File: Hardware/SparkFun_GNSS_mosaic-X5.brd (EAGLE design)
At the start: 63.5 x 50.8 mm, 189 parts, among them J3 MICROSD, J5 USB Female Type C Connector, Q9 20V/0.2A/8MHz/1.2Ω/1Vth, T1 RFCMF1220100M4T, U1 MOSAIC-X5X5, U2 SN74AHC1G125DBVR, U5 3.3V

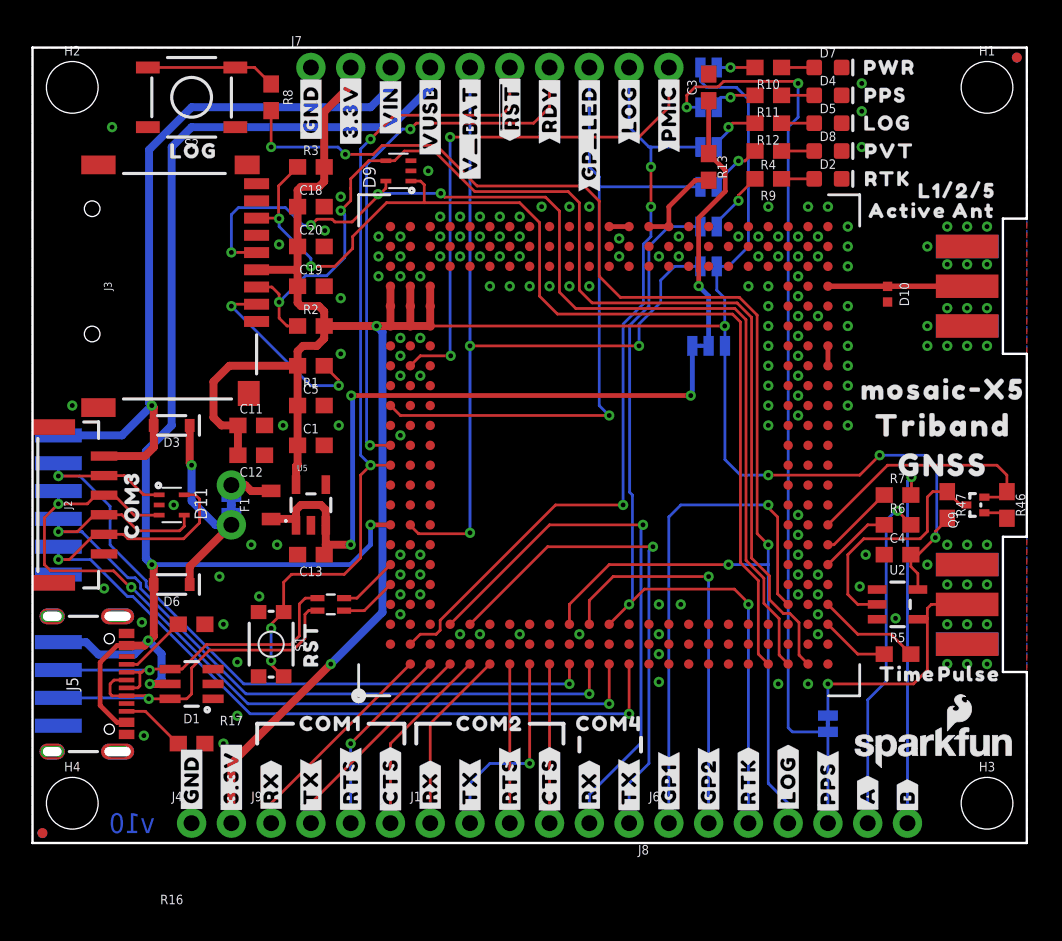
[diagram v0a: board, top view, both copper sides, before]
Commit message: Fix 1.8V net, fix silk, add more ESD protection, add LOG pullup.
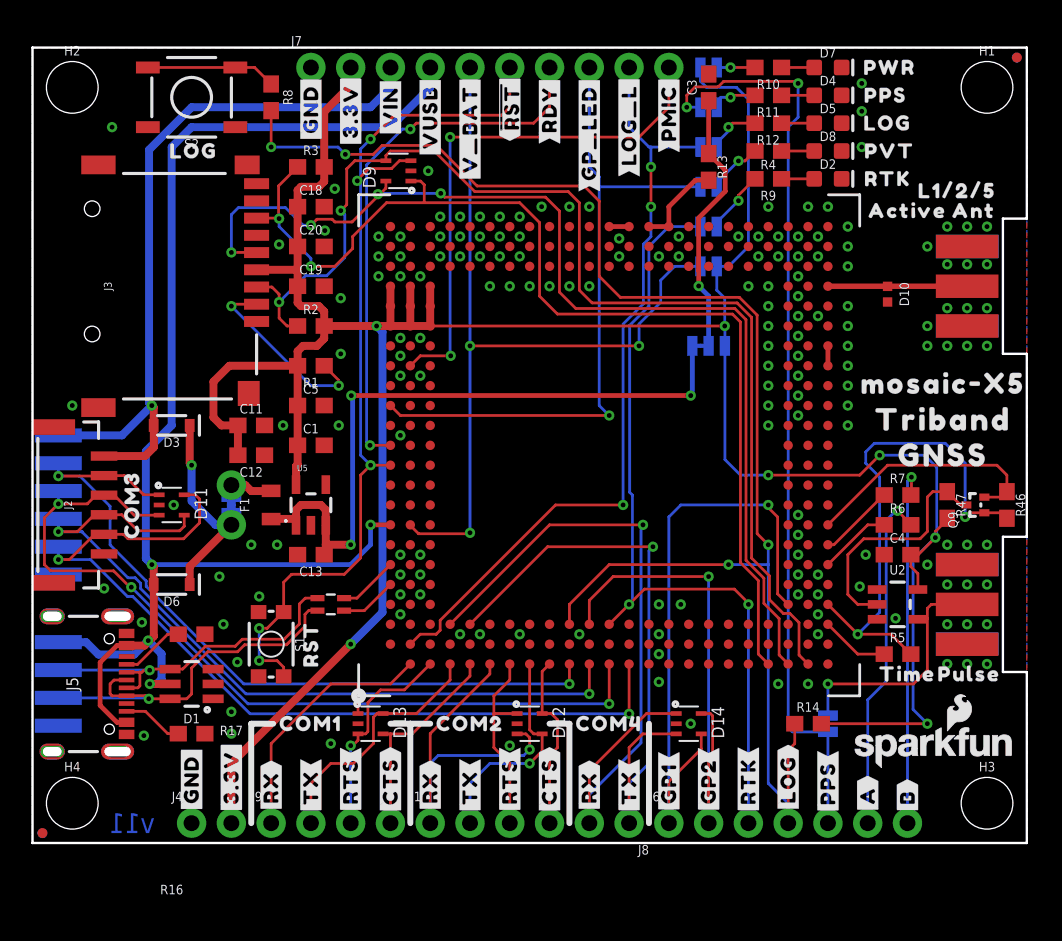
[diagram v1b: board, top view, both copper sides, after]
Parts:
- removed U$105, U$96: (no value), output:#RTS_#5
- removed U$120: (no value), output:#LOG#5
- removed U$126: (no value), output:#LOG_LED_#5
- removed U$127: (no value), output:#PMIC_#6
- removed U$128: (no value), output:#GP_LED_#4
- removed U$129: (no value), output:#RDY_#3
- removed U$148: (no value), output:#EVENTA_#9
- removed U$149: (no value), output:#EVENTB#11
- removed U$151: (no value), output:#GP1_#2
- removed U$153: (no value), output:#GP2_#3
- removed U$155: (no value), output:#LOG_BTN_#5
- removed U$157: (no value), output:#PPS_#7
- added D12, D13, D14: PESDXL4UGUG, SparkFun-DiscreteSemi:SOT353
- added R14: 10k, SparkFun-Resistors:0603
- added U$33: (no value), output:#GP2_#0
- added U$34: (no value), output:#PPS_#0
- added U$35: (no value), output:#LOG_BTN#0
- added U$36: (no value), output:#LOG_L#0
- added U$37: (no value), output:#RDY#0
- added U$38: (no value), output:#GP_LED#0
- added U$39: (no value), output:#LOG_LED#0
- added U$40: (no value), output:#PMIC#0
- added U$41, U$42: (no value), output:#RTS#0
- added U$43: (no value), output:#RTK_#0
- added U$44: (no value), output:#EVENTB#0
- added U$45: (no value), output:MADE_IN_THE_USA0
- U$17: device output:#_RTK#0 -> output:#EVENTA#0
- U$30: device output:MADE_IN_AMERICA0 -> output:#GP1_#0
- moved LOGO1 25.6 mm to (20.3, 13.6)
- moved U$30 23.0 mm to (40.6, 3.56), turned to 270 degrees
- moved U$17 7.75 mm to (53.3, 5.46)
- moved U$83 1.27 mm to (27.9, 7.62)
- moved U$84 1.27 mm to (17.8, 7.62)
- moved U$138 0.64 mm to (58.2, 24.8)
- moved R16 0.64 mm to (10.2, 6.99)
- moved R17 0.63 mm to (10.2, 13.3)
- moved U$19 0.38 mm to (58.2, 29.3)
- moved U$140 0.38 mm to (58.2, 27.1)
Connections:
- removed net ICM-20948-LV_#_1.8V: Q9.1, R46.2
- net !RESET!: now also D9.3
- net 1.8V: now also Q9.1, R46.2
- net 3.3V: now also R14.2
- net COM1_CTS: now also D13.4
- net COM1_RTS: now also D13.3
- net COM1_RX: now also D13.1
- net COM1_TX: now also D13.5
- net COM2_CTS: now also D12.5
- net COM2_RTS: now also D12.1
- net COM2_RX: now also D12.3
- net COM2_TX: now also D12.4
- net COM4_RX: now also D14.1
- net COM4_TX: now also D14.3
- net GND: now also D12.2, D13.2, D14.2
- net GP1: now also D14.4
- net GP2: now also D14.5
- net LOG_BTN: now also R14.1
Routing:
- net 1.8V: track 6.61 -> 32.7 mm, vias 0 -> 2
- net 3.3V: track 169.1 -> 188.7 mm, vias 6 -> 7
- net COM2_RX: track 11.7 -> 23.9 mm, vias 0 -> 1
- net COM4_RX: track 35.4 -> 45.8 mm
- net COM4_TX: track 32.0 -> 40.2 mm
- net GP2: track 25.5 -> 33.3 mm
- net GP1: track 33.1 -> 39.7 mm
- net LOG_BTN: track 89.4 -> 95.9 mm
- net !RESET!: track 53.4 -> 59.1 mm, vias 4 -> 5
- net COM1_RX: track 13.8 -> 18.0 mm
- net COM2_RTS: track 10.2 -> 12.5 mm
- net COM1_TX: track 13.8 -> 16.2 mm
- net ICM-20948-LV_#_1.8V: track 1.58 -> 0.00 mm
- net COM1_CTS: track 12.3 -> 13.5 mm
- net COM1_RTS: track 12.3 -> 13.5 mm
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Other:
- board text added: "v11"
- board text removed: "v10"

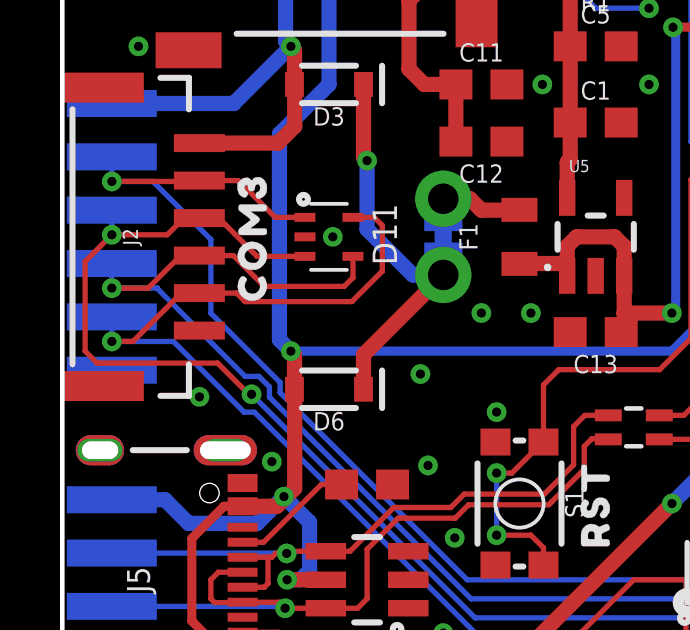
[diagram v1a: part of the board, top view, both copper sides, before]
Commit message: Swap CTS/RTS on COM3 JST connector.
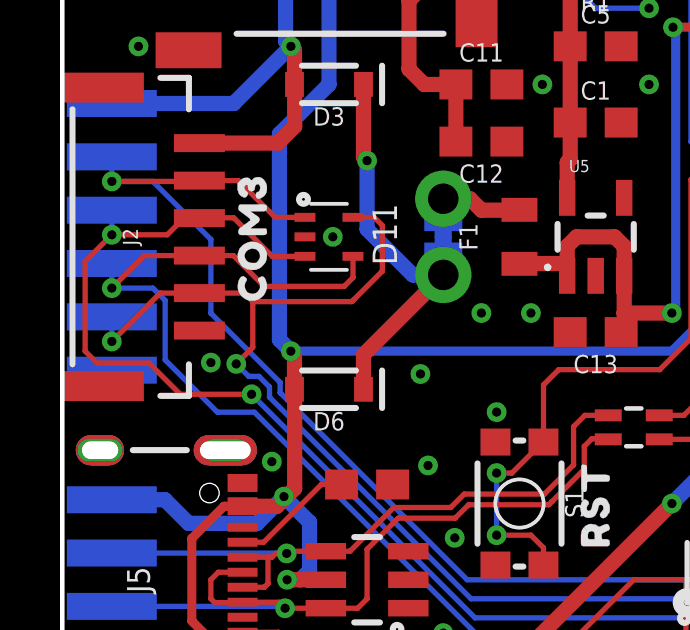
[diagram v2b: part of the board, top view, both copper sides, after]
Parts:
- moved U$12 1.78 mm to (4.19, 18.9)
- moved U$8 1.78 mm to (4.19, 20.7)
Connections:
- net COM3_CTS: now also D11.4, J12.4, J2.4; no longer D11.5, J12.5, J2.5
- net COM3_RTS: now also D11.5, J12.5, J2.5; no longer D11.4, J12.4, J2.4
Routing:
- net COM3_CTS: track 57.4 -> 56.2 mm
- net COM3_RTS: track 50.9 -> 51.1 mm, vias 2 -> 3

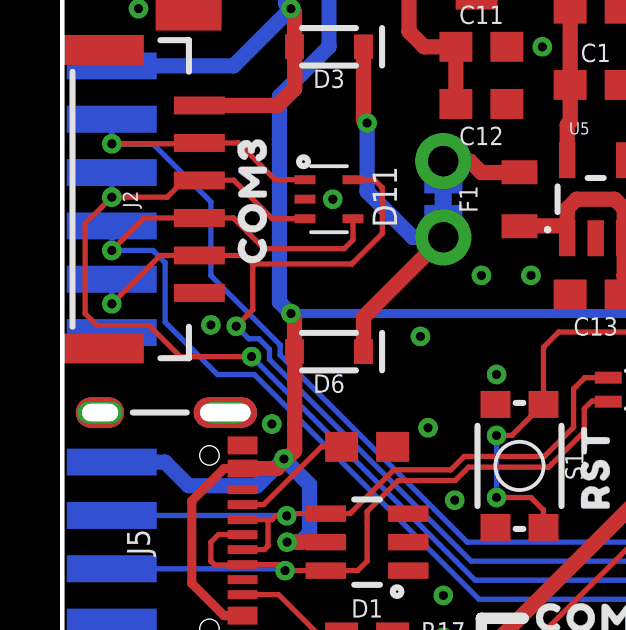
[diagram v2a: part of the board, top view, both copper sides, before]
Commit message: Update board measurements.
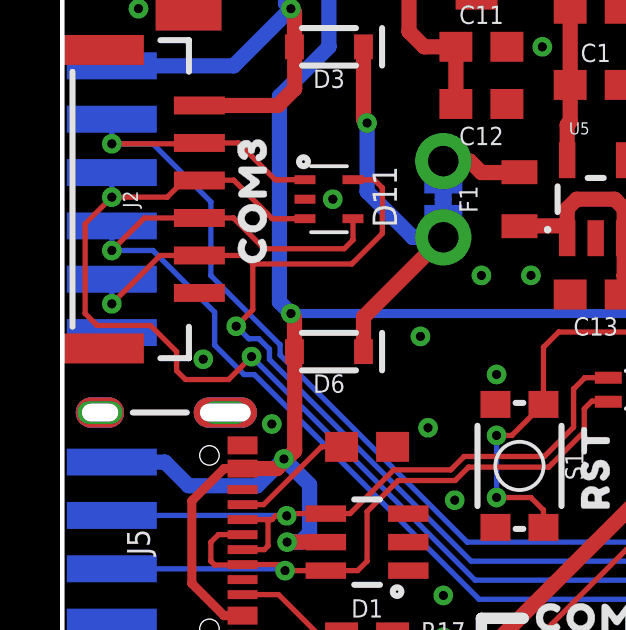
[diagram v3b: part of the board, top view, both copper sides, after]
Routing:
- net COM3_TX: track 54.6 -> 55.6 mm
- net COM3_CTS: track 56.2 -> 55.6 mm
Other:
- board text added: "All dimensions in inches."
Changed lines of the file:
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@@
 <layer number="47" name="Measures" color="7" fill="1" visible="no" active="yes"/>
 <layer number="48" name="Document" color="7" fill="1" visible="no" active="yes"/>
-<layer number="49" name="Reference" color="7" fill="1" visible="no" active="yes"/>
+<layer number="49" name="Reference" color="7" fill="1" visible="yes" active="yes"/>
 <layer number="50" name="dxf" color="7" fill="1" visible="no" active="yes"/>
 <layer number="51" name="tDocu" color="6" fill="1" visible="yes" active="yes"/>
@@
 <wire x1="63.5" y1="39.878" x2="63.5" y2="50.8" width="0.1524" layer="20"/>
 <text x="6.35" y="1.27" size="1.27" layer="16" font="vector" ratio="15" rot="MR180" align="center">v11</text>
-<dimension x1="0" y1="0" x2="0" y2="43.18" x3="-10.16" y3="21.59" textsize="1.778" textratio="15" layer="47" unit="inch"/>
-<dimension x1="0" y1="43.18" x2="43.18" y2="43.18" x3="21.59" y3="49.53" textsize="1.778" textratio="15" layer="47" unit="inch"/>
-<dimension x1="40.64" y1="40.64" x2="2.54" y2="40.64" x3="21.59" y3="45.72" textsize="1.778" textratio="15" layer="47" unit="inch"/>
+<dimension x1="0" y1="0" x2="0" y2="50.8" x3="-10.16" y3="25.4" textsize="1.778" textratio="15" layer="47" unit="inch"/>
+<dimension x1="63.5" y1="50.8" x2="0" y2="50.8" x3="31.75" y3="55.88" textsize="1.778" textratio="15" layer="47" unit="inch"/>
 <dimension x1="2.54" y1="2.54" x2="2.54" y2="0" x3="-6.35" y3="1.27" textsize="1.778" textratio="15" layer="47" unit="inch"/>
-<dimension x1="2.54" y1="2.54" x2="2.54" y2="12.7" x3="-2.54" y3="7.62" textsize="1.778" textratio="15" layer="47" unit="inch"/>
-<dimension x1="1.27" y1="35.56" x2="1.27" y2="43.18" x3="-2.54" y3="39.37" textsize="1.778" textratio="15" layer="47" unit="inch"/>
-<dimension x1="43.18" y1="0" x2="43.18" y2="11.43" x3="52.07" y3="5.715" textsize="1.778" textratio="15" layer="47" unit="inch"/>
-<dimension x1="39.37" y1="11.43" x2="39.37" y2="21.59" x3="52.07" y3="16.51" textsize="1.778" textratio="15" layer="47" unit="inch"/>
-<dimension x1="39.37" y1="21.59" x2="39.37" y2="31.75" x3="52.07" y3="26.67" textsize="1.778" textratio="15" layer="47" unit="inch"/>
-<dimension x1="0" y1="0" x2="8.89" y2="0" x3="4.445" y3="-3.81" textsize="1.778" textratio="15" layer="47" unit="inch"/>
-<dimension x1="8.89" y1="3.81" x2="13.97" y2="3.81" x3="11.43" y3="-3.81" textsize="1.778" textratio="15" layer="47" unit="inch"/>
-<dimension x1="49.53" y1="34.29" x2="43.18" y2="34.29" x3="46.355" y3="36.83" textsize="1.778" textratio="15" layer="47" unit="inch"/>
+<dimension x1="2.54" y1="2.54" x2="2.54" y2="10.16" x3="-2.54" y3="6.35" textsize="1.778" textratio="15" layer="47" unit="inch"/>
+<dimension x1="63.5" y1="0" x2="63.5" y2="15.24" x3="67.31" y3="7.62" textsize="1.778" textratio="15" layer="47" unit="inch"/>
+<dimension x1="63.5" y1="15.24" x2="63.5" y2="35.56" x3="67.310003125" y3="25.4" textsize="1.778" textratio="15" layer="47" unit="inch"/>
+<dimension x1="0" y1="0" x2="10.16" y2="0" x3="5.08" y3="-3.81" textsize="1.778" textratio="15" layer="47" unit="inch"/>
+<dimension x1="10.16" y1="0" x2="12.7" y2="0" x3="11.43" y3="-3.81" textsize="1.778" textratio="15" layer="47" unit="inch"/>
 <text x="21.59" y="-12.7" size="1.778" layer="51" font="vector" ratio="15">N. Seidle</text>
 <text x="99.06" y="31.75" size="1.778" layer="51" font="vector" ratio="15">Finish: ENIG</text>
@@
 <wire x1="22.86" y1="7.62" x2="24.13" y2="7.62" width="0.381" layer="21"/>
 <wire x1="33.02" y1="7.62" x2="34.29" y2="7.62" width="0.381" layer="21"/>
+<dimension x1="0" y1="50.8" x2="17.78" y2="50.8" x3="8.89" y3="53.34" textsize="1.778" textratio="15" layer="47" unit="inch"/>
+<text x="26.67" y="-6.35" size="1.778" layer="47" font="vector" ratio="15">All dimensions in inches.</text>
+<dimension x1="2.54" y1="10.16" x2="2.54" y2="21.59" x3="-2.54" y3="15.875" textsize="1.778" textratio="15" layer="47" unit="inch"/>
+<dimension x1="69.596" y1="38.1" x2="63.5" y2="38.1" x3="66.548" y3="38.988996875" textsize="1.778" textratio="15" layer="47" unit="inch"/>
+<dimension x1="2.54" y1="21.59" x2="2.54" y2="36.449" x3="-2.54" y3="29.0195" textsize="1.778" textratio="15" layer="47" unit="inch"/>
 </plain>
 <attributes>
@@
 <via x="15.621" y="19.05" extent="1-16" drill="0.3048"/>
 <via x="11.938" y="17.018" extent="1-16" drill="0.3048"/>
-<via x="4.953" y="17.399" extent="1-16" drill="0.3048"/>
+<via x="4.699" y="16.256" extent="1-16" drill="0.3048"/>
 <via x="12.192" y="13.97" extent="1-16" drill="0.3048"/>
 <via x="14.478" y="15.748" extent="1-16" drill="0.3048"/>
@@
 <wire x1="8.09" y1="20.94" x2="7" y2="20.94" width="0.1778" layer="1"/>
 <wire x1="1.1603" y1="17.3817" x2="0.762" y2="17.78" width="0.1778" layer="1"/>
-<wire x1="6.308925" y1="16.341925" x2="3.933225" y2="16.341925" width="0.1778" layer="1"/>
-<wire x1="3.933225" y1="16.341925" x2="2.89345" y2="17.3817" width="0.1778" layer="1"/>
-<wire x1="2.89345" y1="17.3817" x2="1.1603" y2="17.3817" width="0.1778" layer="1"/>
+<wire x1="6.308925" y1="16.341925" x2="5.546925" y2="15.579925" width="0.1778" layer="1"/>
 <wire x1="0.762" y1="17.78" x2="0.762" y2="20.77" width="0.1778" layer="1"/>
 <wire x1="0.762" y1="20.77" x2="1.651" y2="21.659" width="0.1778" layer="1"/>
+<wire x1="1.1603" y1="17.3817" x2="2.9383" y2="17.3817" width="0.1778" layer="1"/>
+<wire x1="3.81" y1="16.51" x2="2.9383" y2="17.3817" width="0.1778" layer="1"/>
+<wire x1="5.546925" y1="15.579925" x2="4.105075" y2="15.579925" width="0.1778" layer="1"/>
+<wire x1="4.105075" y1="15.579925" x2="3.81" y2="15.875" width="0.1778" layer="1"/>
+<wire x1="3.81" y1="15.875" x2="3.81" y2="16.51" width="0.1778" layer="1"/>
 </signal>
 <signal name="COM3_RTS">
@@
 <via x="38.1" y="8.255" extent="1-16" drill="0.3048"/>
 <wire x1="38.1" y1="8.255" x2="13.89295" y2="8.255" width="0.1778" layer="16"/>
-<wire x1="6.402925" y1="15.745025" x2="5.172675" y2="15.745025" width="0.1778" layer="16"/>
-<wire x1="5.172675" y1="15.745025" x2="3.429" y2="17.4887" width="0.1778" layer="16"/>
-<wire x1="3.429" y1="17.4887" x2="3.429" y2="19.47216875" width="0.1778" layer="16"/>
+<wire x1="6.402925" y1="15.745025" x2="6.061675" y2="15.745025" width="0.1778" layer="16"/>
+<wire x1="6.061675" y1="15.745025" x2="5.08" y2="16.7267" width="0.1778" layer="16"/>
+<wire x1="5.08" y1="16.7267" x2="5.08" y2="17.82116875" width="0.1778" layer="16"/>
 <wire x1="13.89295" y1="8.255" x2="6.402925" y2="15.745025" width="0.1778" layer="16"/>
 <contactref element="J2" pad="4"/>
@@
 <via x="1.651" y="19.881" extent="1-16" drill="0.3048"/>
 <wire x1="1.651" y1="19.881" x2="1.651" y2="20.701" width="0.1778" layer="16"/>
-<wire x1="3.429" y1="19.47216875" x2="3.02016875" y2="19.881" width="0.1778" layer="16"/>
+<wire x1="5.08" y1="17.82116875" x2="3.02016875" y2="19.881" width="0.1778" layer="16"/>
 <wire x1="3.02016875" y1="19.881" x2="1.651" y2="19.881" width="0.1778" layer="16"/>
 </signal>

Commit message: Change ESD diode on microSD interface.
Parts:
- D9: value PESDXL4UGUG -> DF5A5.6LFU
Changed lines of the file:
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@@
 <layer number="47" name="Measures" color="7" fill="1" visible="no" active="yes"/>
 <layer number="48" name="Document" color="7" fill="1" visible="no" active="yes"/>
-<layer number="49" name="Reference" color="7" fill="1" visible="yes" active="yes"/>
+<layer number="49" name="Reference" color="7" fill="1" visible="no" active="yes"/>
 <layer number="50" name="dxf" color="7" fill="1" visible="no" active="yes"/>
 <layer number="51" name="tDocu" color="6" fill="1" visible="yes" active="yes"/>
@@
 <attribute name="VALUE" x="17.78" y="24.638" size="0.6096" layer="27" font="vector" ratio="20" align="top-center"/>
 </element>
-<element name="D9" library="SparkFun-DiscreteSemi" package="SOT353" value="PESDXL4UGUG" x="23.368" y="42.926" smashed="yes" rot="R90">
+<element name="D9" library="SparkFun-DiscreteSemi" package="SOT353" value="DF5A5.6LFU" x="23.368" y="42.926" smashed="yes" rot="R90">
 <attribute name="NAME" x="21.9145" y="41.82028125" size="0.8128" layer="25" rot="R90"/>
-<attribute name="PROD_ID" value="DIO-19494" x="23.368" y="42.926" size="1.778" layer="27" rot="R90" display="off"/>
+<attribute name="PROD_ID" value="DIO-20454" x="23.368" y="42.926" size="1.778" layer="27" rot="R90" display="off"/>
 <attribute name="VALUE" x="25.908" y="41.656" size="0.8128" layer="27" rot="R90"/>
 </element>

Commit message: Remove "Made in the USA" silk - for foreign PCB manufacture
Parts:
- removed U$45: (no value), output:MADE_IN_THE_USA0
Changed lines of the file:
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@@
 <attribute name="VALUE" x="39.37" y="8.89" size="0.8128" layer="27" rot="R270"/>
 </element>
-<element name="U$45" library="output" package="MADE_IN_THE_USA0" value="" x="19.05" y="11.43" smashed="yes" rot="MR0"/>
 </elements>
 <signals>
